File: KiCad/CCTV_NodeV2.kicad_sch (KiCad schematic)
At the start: 9 parts, among them J1 Solar 6V/10W, J2 Battery (ext, 2× 18650 ||), U1 CN3791, U2 BMS 1S, U3 MT3608, U4 ESP32-S3-DevKitC-1 N16R8, U5 OV7670

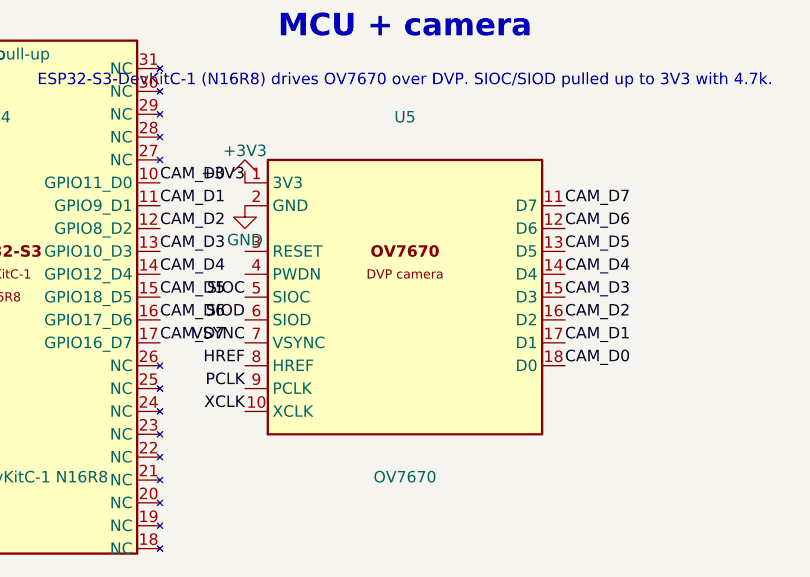
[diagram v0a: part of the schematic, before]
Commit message: Fix OV7670 pin numbering to match actual module (zigzag order)
Previous versions used arbitrary sequential numbering that did NOT
match the real OV7670 module. Corrected based on hardware datasheet.

Correct pinout (2x9 zigzag, L=left col odd, R=right col even):
  Pin 1 (L) = SIOC     Pin 2 (R) = SIOD
  Pin 3 (L) = VSYNC    Pin 4 (R) = HREF
  Pin 5 (L) = PCLK     Pin 6 (R) = XCLK
  Pin 7 (L) = D7       Pin 8 (R) = D6
  Pin 9 (L) = D5       Pin 10(R) = D4
  Pin 11(L) = D3       Pin 12(R) = D2
  Pin 13(L) = D1       Pin 14(R) = D0
  Pin 15(L) = RESET    Pin 16(R) = PWDN
  Pin 17(L) = 3V3      Pin 18(R) = GND

OV7670_Module.kicad_mod:
- Pad positions unchanged (2x9, +-1.27mm columns, 2.54mm row pitch)
- Pad NUMBERS corrected to zigzag (1=top-left, 2=top-right, 3,4 etc.)
- Silk/Fab labels updated with correct signal names per row

CCTV_NodeV2.kicad_sch (OV7670 symbol in lib_symbols):
- All 18 pin numbers renumbered to match physical module
- Pin positions in the symbol drawing are unchanged (same logical
  grouping: power top-left, I2C/sync left, data bus right)
- Nets are still correctly assigned; KiCad will re-resolve pad-to-net
  on next 'Update PCB from Schematic (F8)'
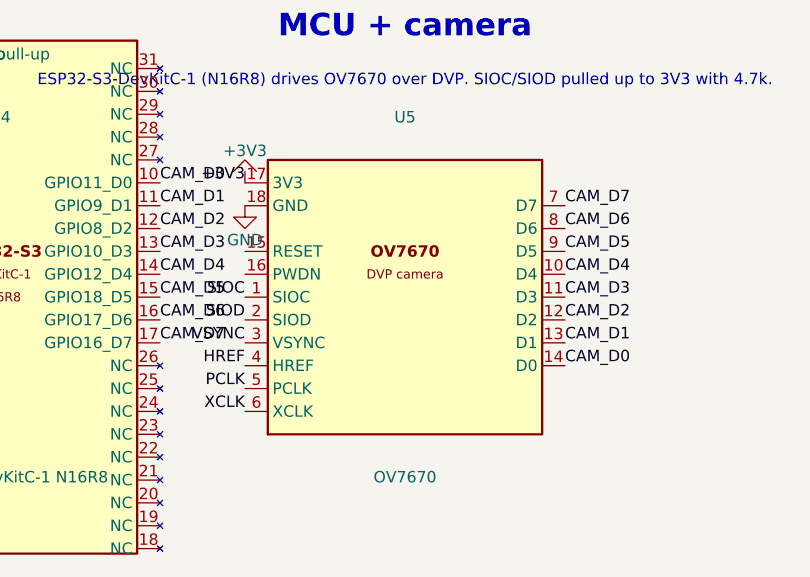
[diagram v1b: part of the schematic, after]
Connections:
- net +3V3: now also U5.17 (3V3); no longer U5.1 (3V3)
- net CAM_D0: now also U5.14 (D0); no longer U5.18 (D0)
- net CAM_D1: now also U5.13 (D1); no longer U5.17 (D1)
- net CAM_D2: now also U5.12 (D2); no longer U5.16 (D2)
- net CAM_D3: now also U5.11 (D3); no longer U5.15 (D3)
- net CAM_D4: now also U5.10 (D4); no longer U5.14 (D4)
- net CAM_D5: now also U5.9 (D5); no longer U5.13 (D5)
- net CAM_D6: now also U5.8 (D6); no longer U5.12 (D6)
- net CAM_D7: now also U5.7 (D7); no longer U5.11 (D7)
- net GND: now also U5.18 (GND); no longer U5.2 (GND)
- net HREF: now also U5.4 (HREF); no longer U5.8 (HREF)
- net PCLK: now also U5.5 (PCLK); no longer U5.9 (PCLK)
- net SIOC: now also U5.1 (SIOC); no longer U5.5 (SIOC)
- net SIOD: now also U5.2 (SIOD); no longer U5.6 (SIOD)
- net VSYNC: now also U5.3 (VSYNC); no longer U5.7 (VSYNC)
- net XCLK: now also U5.6 (XCLK); no longer U5.10 (XCLK)

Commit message: Fix OV7670 pinout: 1=3V3, 2=GND, 3=SIOC ... 17=RESET, 18=PWDN
Corrected to match actual module datasheet (androiderode.com pinout):
  Pin  1 (L row1) = 3V3       Pin  2 (R row1) = GND
  Pin  3 (L row2) = SIOC      Pin  4 (R row2) = SIOD
  Pin  5 (L row3) = VSYNC     Pin  6 (R row3) = HREF
  Pin  7 (L row4) = PCLK      Pin  8 (R row4) = XCLK
  Pin  9 (L row5) = D7        Pin 10 (R row5) = D6
  Pin 11 (L row6) = D5        Pin 12 (R row6) = D4
  Pin 13 (L row7) = D3        Pin 14 (R row7) = D2
  Pin 15 (L row8) = D1        Pin 16 (R row8) = D0
  Pin 17 (L row9) = RESET     Pin 18 (R row9) = PWDN

Previous incorrect version (last commit) had 3V3 at pin 17, SIOC
at pin 1. This version is now correct.
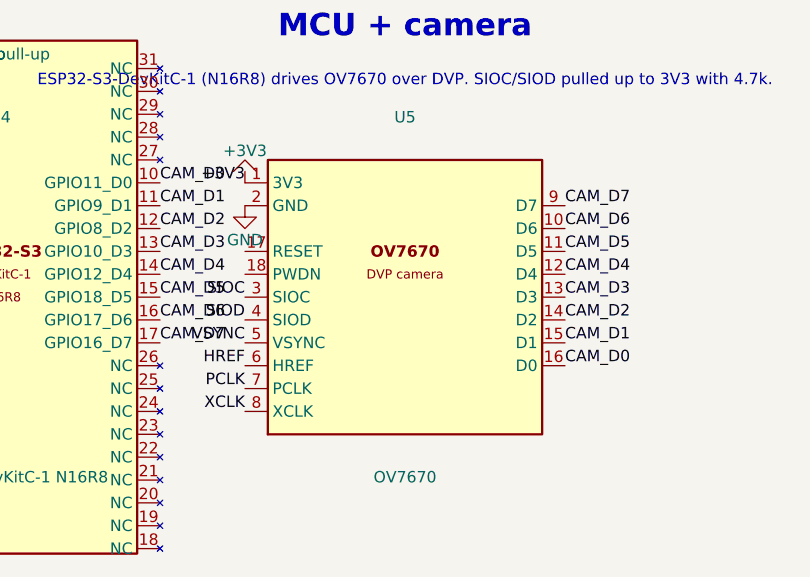
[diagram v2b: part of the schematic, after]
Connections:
- net +3V3: now also U5.1 (3V3); no longer U5.17 (3V3)
- net CAM_D0: now also U5.16 (D0); no longer U5.14 (D0)
- net CAM_D1: now also U5.15 (D1); no longer U5.13 (D1)
- net CAM_D2: now also U5.14 (D2); no longer U5.12 (D2)
- net CAM_D3: now also U5.13 (D3); no longer U5.11 (D3)
- net CAM_D4: now also U5.12 (D4); no longer U5.10 (D4)
- net CAM_D5: now also U5.11 (D5); no longer U5.9 (D5)
- net CAM_D6: now also U5.10 (D6); no longer U5.8 (D6)
- net CAM_D7: now also U5.9 (D7); no longer U5.7 (D7)
- net GND: now also U5.2 (GND); no longer U5.18 (GND)
- net HREF: now also U5.6 (HREF); no longer U5.4 (HREF)
- net PCLK: now also U5.7 (PCLK); no longer U5.5 (PCLK)
- net SIOC: now also U5.3 (SIOC); no longer U5.1 (SIOC)
- net SIOD: now also U5.4 (SIOD); no longer U5.2 (SIOD)
- net VSYNC: now also U5.5 (VSYNC); no longer U5.3 (VSYNC)
- net XCLK: now also U5.8 (XCLK); no longer U5.6 (XCLK)

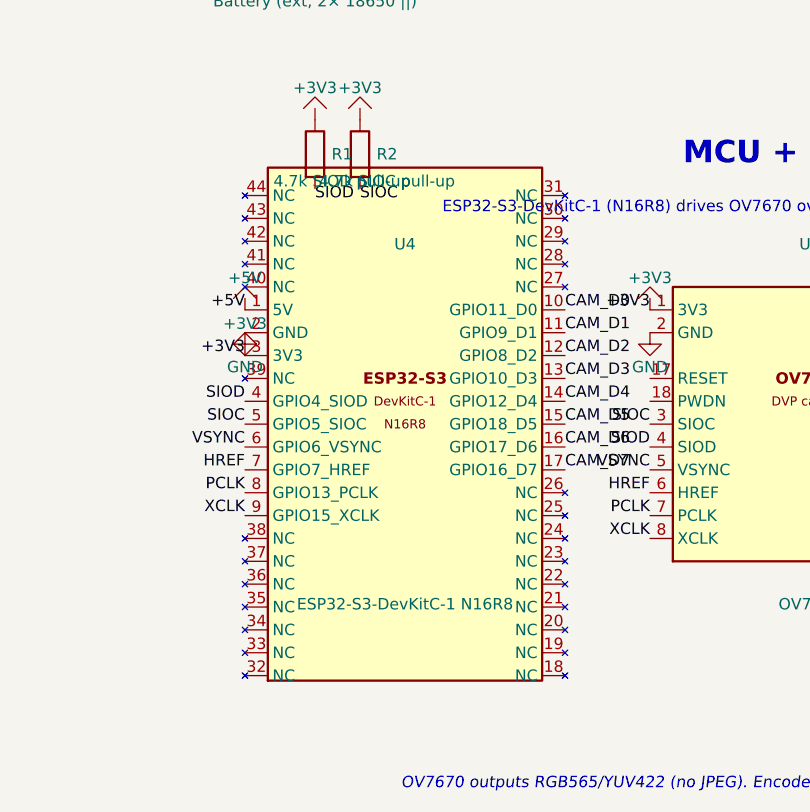
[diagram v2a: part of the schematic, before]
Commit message: Fix ESP32-S3-DevKitC-1 layout to match physical board (OceanLabz pinout)
Footprint (ESP32-S3-DevKitC-1.kicad_mod):
  44 pads at correct physical y-positions (2.54mm pitch, y=-27.94 to +25.40)
  Left col pads 1-22 (x=-11.43):
    1=3V3, 2=3V3, 3=RST, 4=GPIO4, 5=GPIO5, 6=GPIO6, 7=GPIO7,
    8=GPIO15, 9=GPIO16, 10=GPIO17, 11=GPIO18, 12=GPIO8, 13=GPIO3,
    14=GPIO46, 15=GPIO9, 16=GPIO10, 17=GPIO11, 18=GPIO12, 19=GPIO13,
    20=GPIO14, 21=5V0, 22=GND
  Right col pads 23-44 (x=+11.43):
    23=GND, 24=GPIO43, 25=GPIO44, 26=GPIO1, 27=GPIO2, 28=GPIO42,
    29=GPIO41, 30=GPIO40, 31=GPIO39, 32=GPIO38(RGB), 33=GPIO37,
    34=GPIO36, 35=GPIO35, 36=GPIO0(BOOT), 37=GPIO45, 38=GPIO48,
    39=GPIO47, 40=GPIO21, 41=GPIO20, 42=GPIO19, 43=GND, 44=GND
  Silk labels on both columns, notch on pin 1 (top-left, 3V3)

Schematic symbol (CCTV_NodeV2.kicad_sch):
  All 44 pins drawn at correct physical y-positions to match board image
  Left side functional pins (nets): 1=+3V3, 4=SIOD, 5=SIOC, 6=VSYNC,
    7=HREF, 8=XCLK, 9=D7, 10=D6, 11=D5, 12=D2, 15=D1, 16=D3, 17=D0,
    18=D4, 19=PCLK, 21=+5V, 22=GND
  NC pins: 2(3V3_2), 3(RST), 13(GPIO3), 14(GPIO46), 20(GPIO14),
    all right-column pins 23-44
  Placed U4 instance expanded from 17 to 44 pin-UUID entries
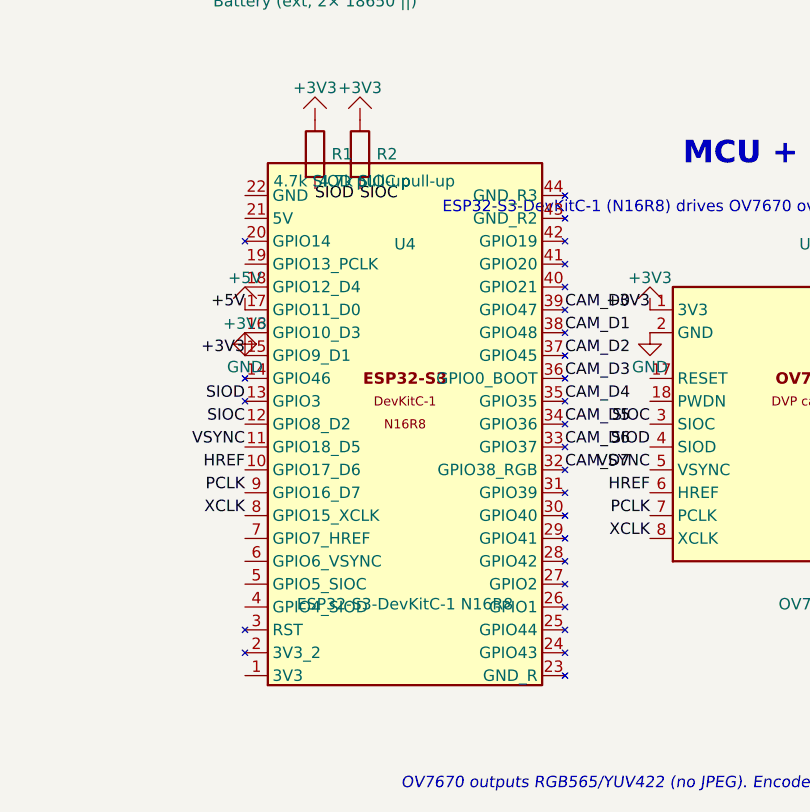
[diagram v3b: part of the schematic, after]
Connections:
- net +3V3: now also U4.15 (GPIO9_D1); no longer U4.3 (3V3)
- net +5V: now also U4.17 (GPIO11_D0); no longer U4.1 (5V)
- net CAM_D0: now also U4.39 (GPIO47); no longer U4.10 (GPIO11_D0)
- net CAM_D1: now also U4.38 (GPIO48); no longer U4.11 (GPIO9_D1)
- net CAM_D2: now also U4.37 (GPIO45); no longer U4.12 (GPIO8_D2)
- net CAM_D3: now also U4.36 (GPIO0_BOOT); no longer U4.13 (GPIO10_D3)
- net CAM_D4: now also U4.35 (GPIO35); no longer U4.14 (GPIO12_D4)
- net CAM_D5: now also U4.34 (GPIO36); no longer U4.15 (GPIO18_D5)
- net CAM_D6: now also U4.33 (GPIO37); no longer U4.16 (GPIO17_D6)
- net CAM_D7: now also U4.32 (GPIO38_RGB); no longer U4.17 (GPIO16_D7)
- net GND: now also U4.16 (GPIO10_D3); no longer U4.2 (GND)
- net HREF: now also U4.10 (GPIO17_D6); no longer U4.7 (GPIO7_HREF)
- net PCLK: now also U4.9 (GPIO16_D7); no longer U4.8 (GPIO13_PCLK)
- net SIOC: now also U4.12 (GPIO8_D2); no longer U4.5 (GPIO5_SIOC)
- net SIOD: now also U4.13 (GPIO3); no longer U4.4 (GPIO4_SIOD)
- net VSYNC: now also U4.11 (GPIO18_D5); no longer U4.6 (GPIO6_VSYNC)
- net XCLK: now also U4.8 (GPIO15_XCLK); no longer U4.9 (GPIO15_XCLK)
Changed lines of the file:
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@@
 		(pin "16")
 		(pin "17")
+		(pin "18")
+		(pin "19")
+		(pin "20")
+		(pin "21")
+		(pin "22")
+		(pin "23")
+		(pin "24")
+		(pin "25")
+		(pin "26")
+		(pin "27")
+		(pin "28")
+		(pin "29")
+		(pin "30")
+		(pin "31")
+		(pin "32")
+		(pin "33")
+		(pin "34")
+		(pin "35")
+		(pin "36")
+		(pin "37")
+		(pin "38")
+		(pin "39")
+		(pin "40")
+		(pin "41")
+		(pin "42")
+		(pin "43")
+		(pin "44")
 		(instances
 			(project "CCTV_NodeV2"

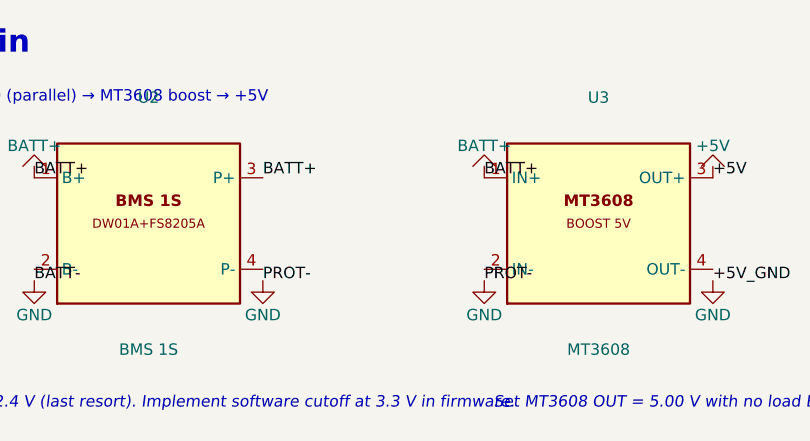
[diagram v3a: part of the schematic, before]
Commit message: Fix BMS → MT3608 power path: add P+ net, remove BATT+ bypass
The MT3608 boost converter was incorrectly connected directly to the
BATT+ net (raw battery positive), bypassing the 1S BMS protection.

Correct power flow (battery → BMS → MT3608 → 5V → ESP32):
  Battery J2 +  → BATT+  → BMS B+  (cell side, charging via CN3791)
  BMS P+ output → P+    → MT3608 IN+  (protected, load side)
  BMS P- output → PROT- → MT3608 IN-  (already correct)

Schematic (CCTV_NodeV2.kicad_sch):
- Removed stray BATT+ power flag at MT3608 IN+ (167.3, 64.92)
- Renamed net label at BMS P+ pin (142.7, 64.92): BATT+ → P+
- Renamed net label at MT3608 IN+ pin (167.3, 64.92): BATT+ → P+

PCB (CCTV_NodeV2.kicad_pcb):
- BMS pad 3 (P+ output): net BATT+ → P+
- MT3608 pad 1 (IN+):    net BATT+ → P+

The BMS over-discharge cutoff (DW01A ~2.4V trip) now actually
disconnects the MT3608 load via P-/PROT-. The P+ net is always the
same voltage as BATT+ when the BMS is conducting (1S BMS has no
MOSFET in the positive path), but labelling them separately in the
schematic makes the protection intent explicit.
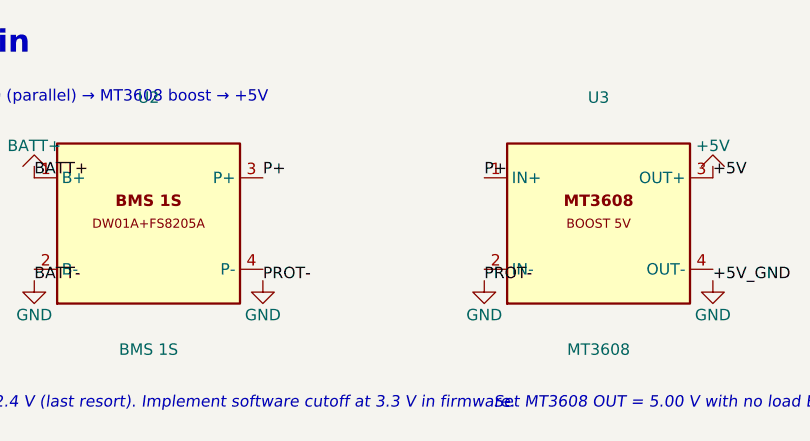
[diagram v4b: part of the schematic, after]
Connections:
- net BATT+: no longer U2.3 (P+), U3.1 (IN+)
- new net P+: U2.3 (P+), U3.1 (IN+)
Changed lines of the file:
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@@
-	)
-	(symbol
-		(lib_id "CCTV2:BATT+")
-		(at 167.3 64.92 0)
-		(unit 1)
-		(in_bom yes)
-		(on_board yes)
-		(dnp no)
-		(property "Reference" "#PWR08"
-			(at 167.3 61.11 0)
-			(hide yes)
-		)
-		(property "Value" "BATT+"
-			(at 167.3 61.36 0)
-		)
-		(pin "1")
-		(instances
-			(project "CCTV_NodeV2"
-				(path "/b0c0d0e0-0001-4000-8000-000000000001"
-					(reference "#PWR08")
-					(unit 1)
-				)
-			)
-		)
 	)
 	(symbol
@@
 		(effects (font (size 1.27 1.27)) (justify left top))
 	)
-	(label "BATT+"
+	(label "P+"
 		(at 167.3 64.92 0)
 		(effects (font (size 1.27 1.27)) (justify left bottom))
@@
 		(effects (font (size 1.27 1.27)) (justify left top))
 	)
-	(label "BATT+"
+	(label "P+"
 		(at 142.7 64.92 0)
 		(effects (font (size 1.27 1.27)) (justify left bottom))

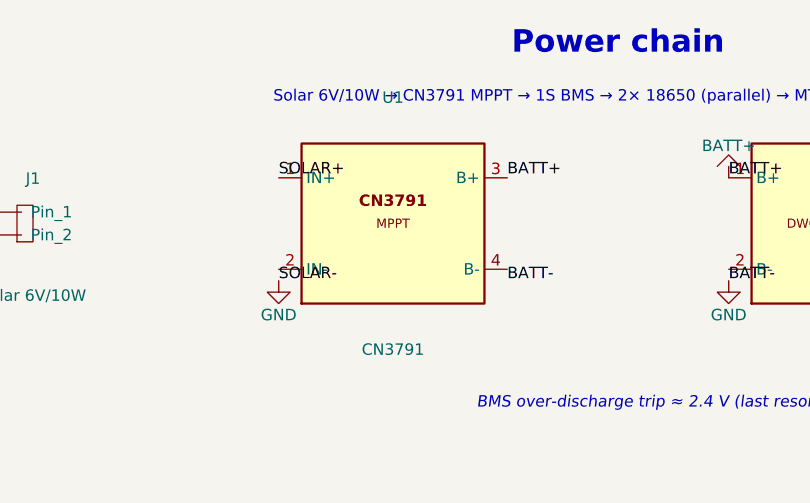
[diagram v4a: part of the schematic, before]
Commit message: Redesign CN3791 footprint: single-row 4-hole + correct pinout
Physical module has 4 holes in a single row (not 2x2), labelled
left-to-right: VIN | GND | GND | BAT

CN3791_Module.kicad_mod (footprint):
- Changed from wide 2x2 layout (x=+-20mm) to single row
- 4 pads at 2.54mm pitch: x = -3.81, -1.27, +1.27, +3.81, all y=0
- PCB outline: 35x17mm body on F.Fab + F.SilkS
- Courtyard: 36.4x18.4mm
- Silk labels: VIN / GND / GND / BAT above each pad
- Pin 1 marker + orientation notch top-left
- CN3791 IC body placeholder + LED circle on F.Fab

CCTV_NodeV2.kicad_sch (schematic symbol fix):
- CN3791 pin 3 was B+/BAT+ → now GND (physical pad 3 = GND)
- CN3791 pin 4 was B-/BAT- → now BAT+ (physical pad 4 = BAT)
- Net labels at U1 right side already correct positionally:
    BATT+ at upper-right → connects to new pin 4 (BAT+)
    BATT- at lower-right → connects to new pin 3 (GND)

CCTV_NodeV2.kicad_pcb (U1 pad positions + net swap):
  Pad 1: at (-3.81, 0)  net SOLAR+   (was -20,-2.5)
  Pad 2: at (-1.27, 0)  net SOLAR-   (was -20,+2.5)
  Pad 3: at (+1.27, 0)  net BATT-    (was +20,-2.5, net was BATT+!)
  Pad 4: at (+3.81, 0)  net BATT+    (was +20,+2.5, net was BATT-!)
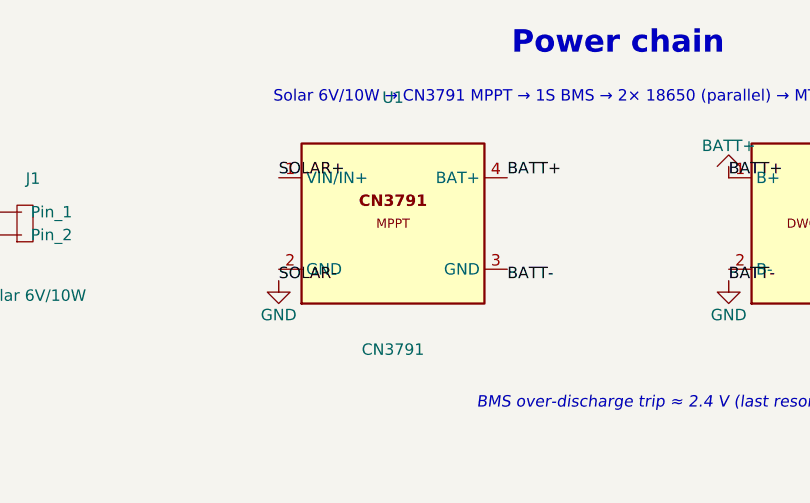
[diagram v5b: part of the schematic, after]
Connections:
- net BATT+: now also U1.4 (BAT+); no longer U1.3 (B+)
- net BATT-: now also U1.3 (GND); no longer U1.4 (B-)

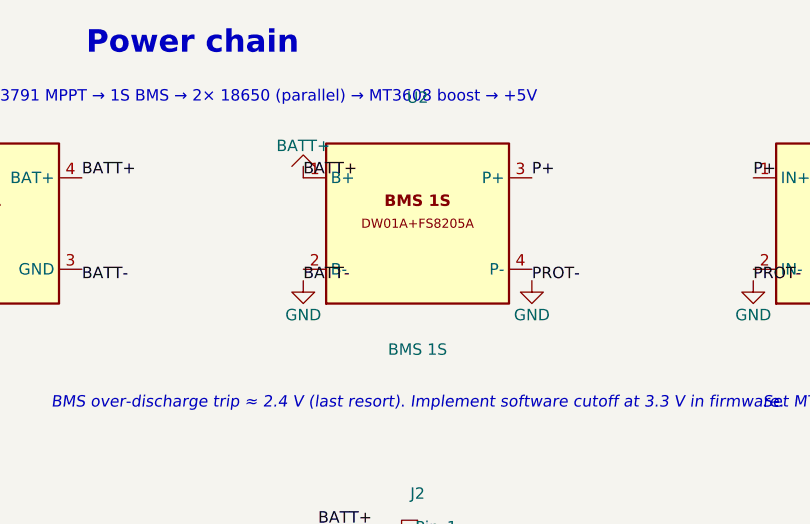
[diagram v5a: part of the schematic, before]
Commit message: Replace U2 BMS from DW01A+FS8205A to TC4056A_BMS_Module
Replaces the standalone 1S BMS (DW01A + FS8205A) with the TC4056A
combined USB charger + BMS protection module on U2.

Schematic (CCTV_NodeV2.kicad_sch):
- Added CCTV2:TC4056A_BMS lib symbol (6 pins):
    Pin 1 = IN+  (USB 5V charging input)  → NC marker
    Pin 2 = IN-  (USB GND)               → GND symbol
    Pin 3 = B+   (battery positive)       → BATT+ (same position as old BMS pin1)
    Pin 4 = B-   (battery negative)       → BATT-/GND (same position as old BMS pin2)
    Pin 5 = OUT+ (BMS protected output +) → P+    (same position as old BMS pin3)
    Pin 6 = OUT- (BMS protected output -) → PROT- (same position as old BMS pin4)
- Replaced U2 lib_id BMS_1S → TC4056A_BMS
- Updated U2 footprint: BMS_1S_DW01A_FS8205A → TC4056A_BMS_Module
- Added GND power symbol for IN- at (117.3, 60.65)
- Added no_connect flag at IN+ (117.3, 57.3)
  (connect a USB cable / J connector here for USB charging)

PCB (CCTV_NodeV2.kicad_pcb):
- Replaced entire U2 footprint block with TC4056A_BMS_Module geometry
  (26x17mm body, 6 pads single row at 2.54mm pitch)
- Pad nets: 1=NC, 2=GND, 3=BATT+, 4=BATT-, 5=P+, 6=PROT-
- Existing traces to old 4-pad BMS pads are now airwires — re-route
  with Freerouting or manually in pcbnew
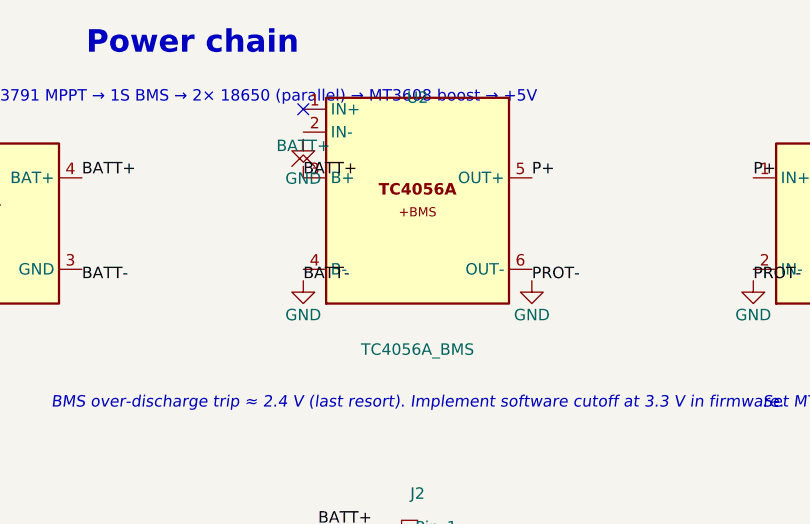
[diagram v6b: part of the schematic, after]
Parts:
- U2: value BMS 1S -> TC4056A_BMS; footprint CCTV_RPi4:BMS_1S_DW01A_FS8205A -> CCTV_RPi4:TC4056A_BMS_Module; symbol CCTV2:BMS_1S -> CCTV2:TC4056A_BMS
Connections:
- net BATT+: now also U2.3 (B+); no longer U2.1 (B+)
- net BATT-: now also U2.4 (B-); no longer U2.2 (B-)
- net P+: now also U2.5 (OUT+); no longer U2.3 (P+)
- net PROT-: now also U2.6 (OUT-); no longer U2.4 (P-)
- no-connect marks 0 -> 1
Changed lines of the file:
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@@
 	)
 	(symbol
-		(lib_id "CCTV2:BMS_1S")
+		(lib_id "CCTV2:TC4056A_BMS")
 		(at 130 70 0)
 		(unit 1)
@@
 			(at 130 56 0)
 		)
-		(property "Value" "BMS 1S"
+		(property "Value" "TC4056A_BMS"
 			(at 130 84 0)
 		)
-		(property "Footprint" "CCTV_RPi4:BMS_1S_DW01A_FS8205A"
+		(property "Footprint" "CCTV_RPi4:TC4056A_BMS_Module"
 			(at 0 0 0)
 			(hide yes)
@@
 		(pin "3")
 		(pin "4")
+		(pin "5")
+		(pin "6")
 		(instances
 			(project "CCTV_NodeV2"
@@
 	)
 	(symbol
+		(lib_id "CCTV2:GND")
+		(at 117.3 60.65 0)
+		(unit 1)
+		(in_bom yes)
+		(on_board yes)
+		(dnp no)
+		(property "Reference" "#PWR_IN_NEG"
+			(at 117.3 67 0)
+			(hide yes)
+		)
+		(property "Value" "GND"
+			(at 117.3 65 0)
+		)
+		(pin "1")
+		(instances
+			(project "CCTV_NodeV2"
+				(path "/b0c0d0e0-0001-4000-8000-000000000001"
+					(reference "#PWR_IN_NEG")
+					(unit 1)
+				)
+			)
+		)
+	)
+	(no_connect
+		(at 117.3 57.3)
+		(uuid "nc000001-0000-0000-0000-000000000001")
+	)
+	(symbol
